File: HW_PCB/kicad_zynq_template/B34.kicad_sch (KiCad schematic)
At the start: 7 parts, among them U2 XA7Z020-1CLG400I

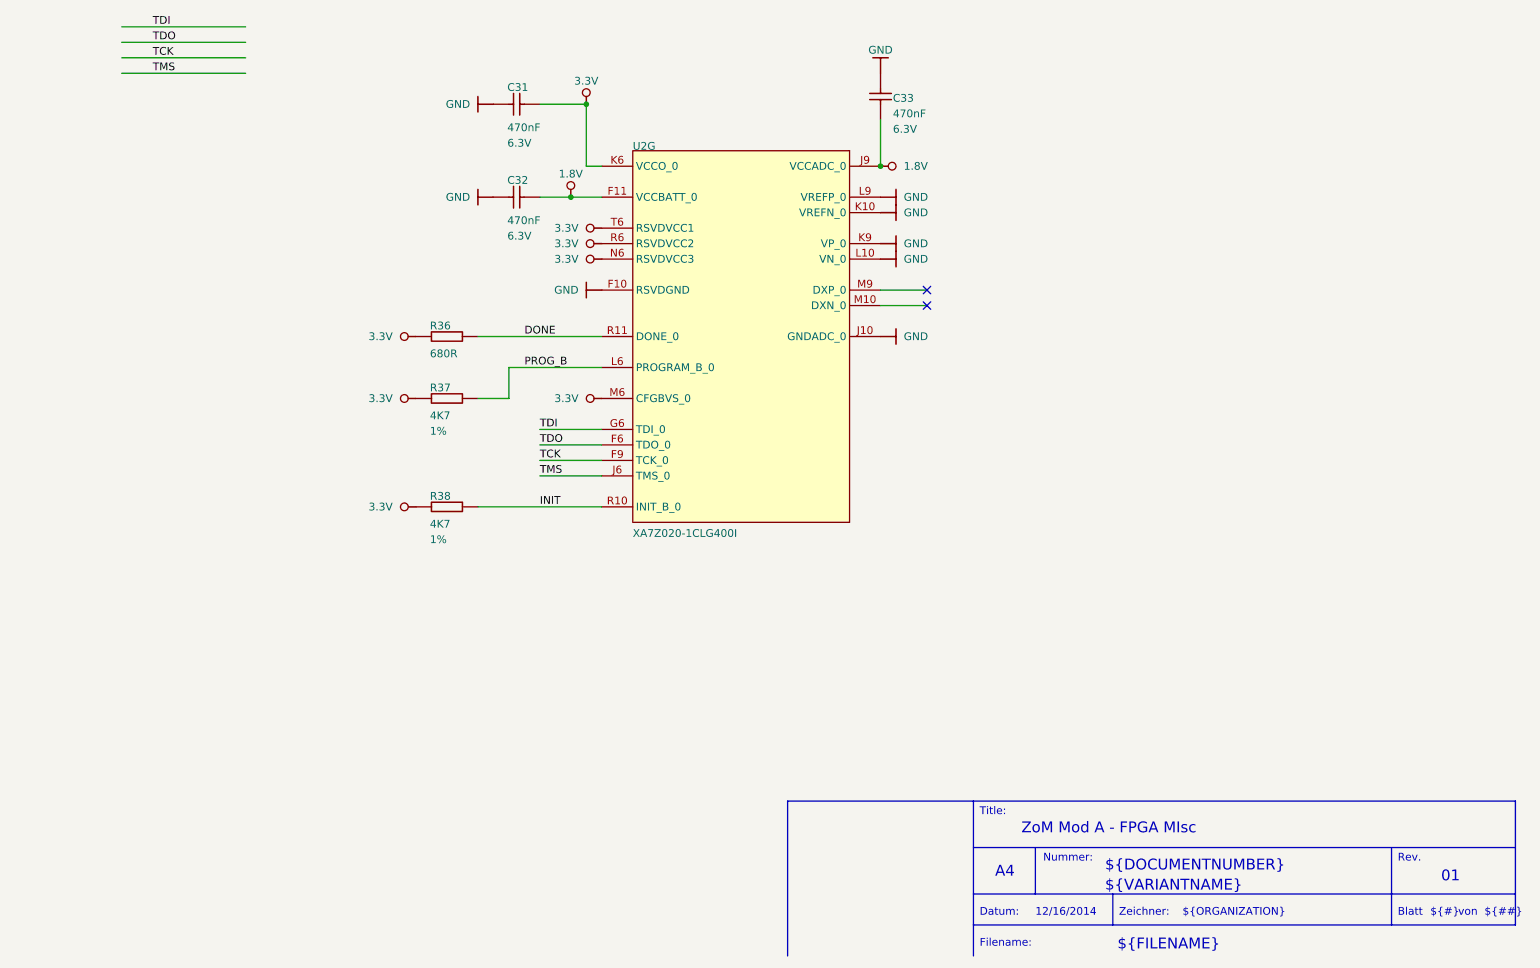
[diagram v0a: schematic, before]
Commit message: pcbs tidied up
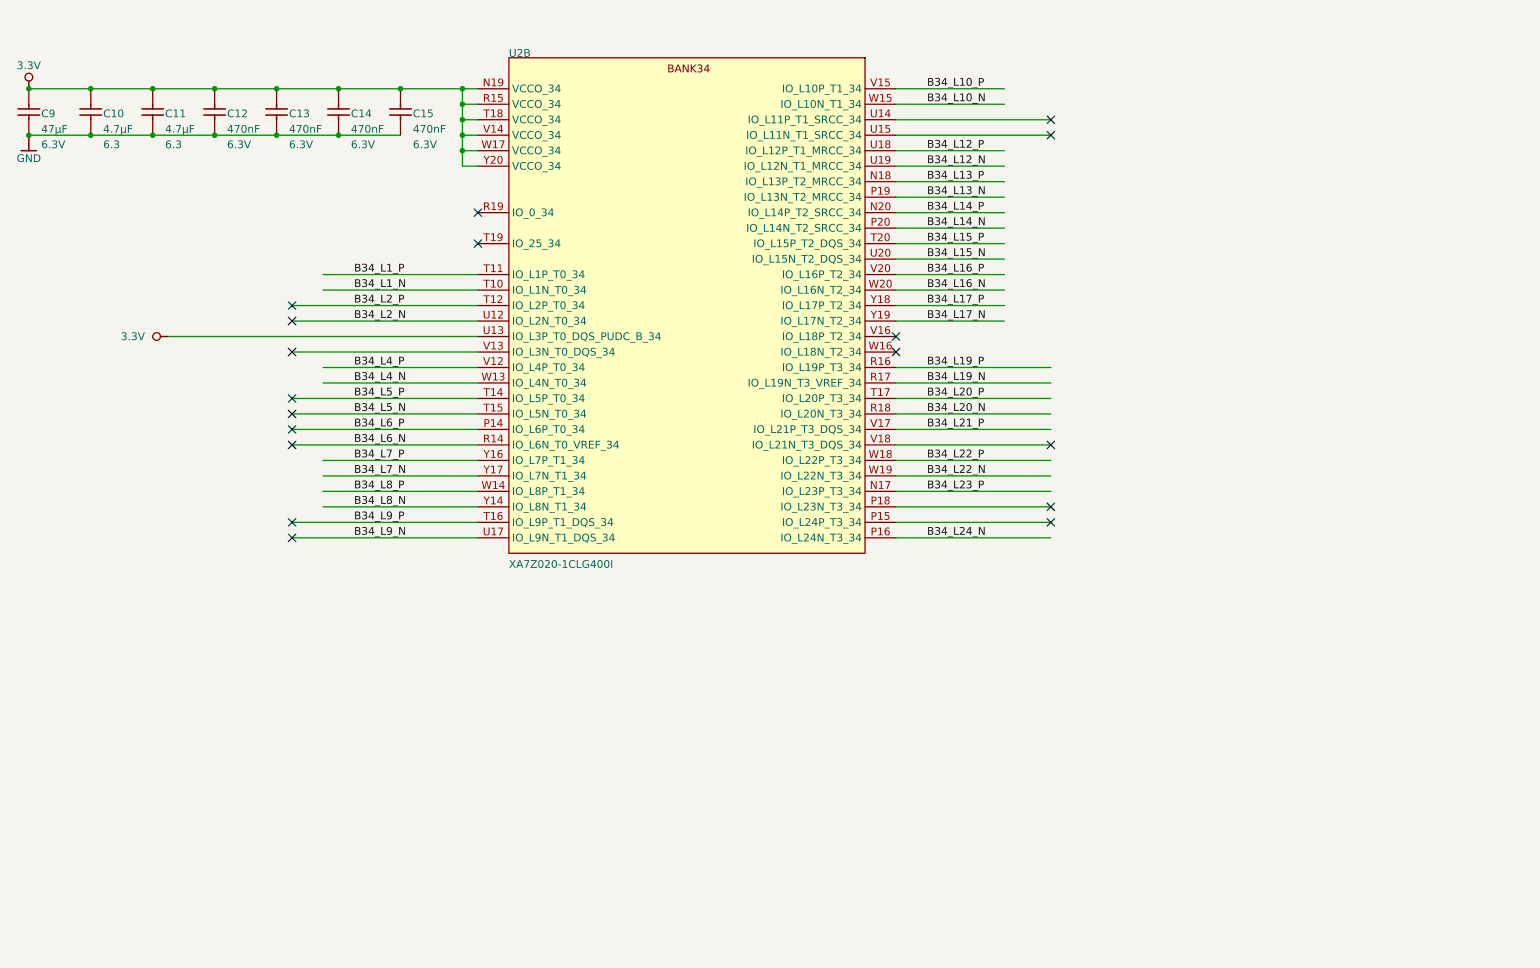
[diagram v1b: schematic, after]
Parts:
- removed C31: 470nF, symbol TE0719-altium-import:FPGA-Misc_1_CAP-NP
- removed C32: 470nF, CAPC0603X33N, symbol TE0719-altium-import:FPGA-Misc_1_CAP-NP
- removed C33: 470nF, CAPC0603X33N, symbol TE0719-altium-import:FPGA-Misc_0_CAP-NP
- removed R36: 680R, RESC1005X40N, symbol TE0719-altium-import:FPGA-Misc_1_RES
- removed R37: 4K7, RESC0603X26N, symbol TE0719-altium-import:FPGA-Misc_3_RES
- removed R38: 4K7, symbol TE0719-altium-import:FPGA-Misc_3_RES
- removed U2: XA7Z020-1CLG400I, BGA400C80P20X20_1700X1700X160N, symbol TE0719-altium-import:FPGA-Misc_0_XC7Z020-2CLG400C
- added C10, C11: 4.7µF, CAPC1005X60N, symbol TE0719-altium-import:B34_0_CAP-NP
- added C12, C13, C14, C15: 470nF, CAPC0603X33N, symbol TE0719-altium-import:B34_0_CAP-NP
- added C9: 47µF, CAPC3216X180N, symbol TE0719-altium-import:B34_0_CAP-NP
- added U2: XA7Z020-1CLG400I, BGA400C80P20X20_1700X1700X160N, symbol TE0719-altium-import:B34_0_XC7Z020-2CLG400C
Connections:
- net 3.3V: now also C10.1, C11.1, C12.1, C13.1, C14.1, C15.1, C9.1, U2.N19 (VCCO_34), U2.R15 (VCCO_34), U2.T18 (VCCO_34), U2.U13 (IO_L3P_T0_DQS_PUDC_B_34), U2.V14 (VCCO_34), U2.W17 (VCCO_34), U2.Y20 (VCCO_34)
- net GND: now also C10.2, C11.2, C12.2, C13.2, C14.2, C15.2, C9.2
- new net B34_L10_N: U2.W15 (IO_L10N_T1_34)
- new net B34_L10_P: U2.V15 (IO_L10P_T1_34)
- new net B34_L12_N: U2.U19 (IO_L12N_T1_MRCC_34)
- new net B34_L12_P: U2.U18 (IO_L12P_T1_MRCC_34)
- new net B34_L13_N: U2.P19 (IO_L13N_T2_MRCC_34)
- new net B34_L13_P: U2.N18 (IO_L13P_T2_MRCC_34)
- new net B34_L14_N: U2.P20 (IO_L14N_T2_SRCC_34)
- new net B34_L14_P: U2.N20 (IO_L14P_T2_SRCC_34)
- new net B34_L15_N: U2.U20 (IO_L15N_T2_DQS_34)
- new net B34_L15_P: U2.T20 (IO_L15P_T2_DQS_34)
- new net B34_L16_N: U2.W20 (IO_L16N_T2_34)
- new net B34_L16_P: U2.V20 (IO_L16P_T2_34)
- new net B34_L17_N: U2.Y19 (IO_L17N_T2_34)
- new net B34_L17_P: U2.Y18 (IO_L17P_T2_34)
- new net B34_L19_N: U2.R17 (IO_L19N_T3_VREF_34)
- new net B34_L19_P: U2.R16 (IO_L19P_T3_34)
- new net B34_L1_N: U2.T10 (IO_L1N_T0_34)
- new net B34_L1_P: U2.T11 (IO_L1P_T0_34)
- new net B34_L20_N: U2.R18 (IO_L20N_T3_34)
- new net B34_L20_P: U2.T17 (IO_L20P_T3_34)
- new net B34_L21_P: U2.V17 (IO_L21P_T3_DQS_34)
- new net B34_L22_N: U2.W19 (IO_L22N_T3_34)
- new net B34_L22_P: U2.W18 (IO_L22P_T3_34)
- new net B34_L23_P: U2.N17 (IO_L23P_T3_34)
- new net B34_L24_N: U2.P16 (IO_L24N_T3_34)
- new net B34_L2_N: U2.U12 (IO_L2N_T0_34)
- new net B34_L2_P: U2.T12 (IO_L2P_T0_34)
- new net B34_L4_N: U2.W13 (IO_L4N_T0_34)
- new net B34_L4_P: U2.V12 (IO_L4P_T0_34)
- new net B34_L5_N: U2.T15 (IO_L5N_T0_34)
- new net B34_L5_P: U2.T14 (IO_L5P_T0_34)
- new net B34_L6_N: U2.R14 (IO_L6N_T0_VREF_34)
- new net B34_L6_P: U2.P14 (IO_L6P_T0_34)
- new net B34_L7_N: U2.Y17 (IO_L7N_T1_34)
- new net B34_L7_P: U2.Y16 (IO_L7P_T1_34)
- new net B34_L8_N: U2.Y14 (IO_L8N_T1_34)
- new net B34_L8_P: U2.W14 (IO_L8P_T1_34)
- new net B34_L9_N: U2.U17 (IO_L9N_T1_DQS_34)
- new net B34_L9_P: U2.T16 (IO_L9P_T1_DQS_34)
- no-connect marks 2 -> 18
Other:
- note removed: "${##}"
- note removed: "${#}"
- note removed: "${DOCUMENTNUMBER}"
- note removed: "${FILENAME}"
- note removed: "${ISSUE_DATE}"
- note removed: "${ORGANIZATION}"
- note removed: "${REVISION}"
- note removed: "${TITLE}"
- note removed: "${VARIANTNAME}"
- note removed: "A4"
- note removed: "Blatt"
- note removed: "Datum:"
- note removed: "Filename:"
- note removed: "Nummer:"
- note removed: "Rev."
- note removed: "Title:"
- note removed: "Zeichner:"
- note removed: "von"
- title: ZoM Mod A - FPGA MIsc -> ZoM Mod A - FPGA Bank 34
